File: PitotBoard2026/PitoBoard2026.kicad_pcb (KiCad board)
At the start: 2 copper layers, 8.5 x 5.5 mm, 57 parts, among them J1 RJ25, J2 ICSP, J3 Conn_01x04_Socket, J4 Conn_01x04_Pin, J5 Conn_01x04_Socket, J6 Conn_01x04_Pin, SW1 RST, U1 ATmega328PB-A, U10 MCP25625-x-SS, U2 AP7375, U4 SLIP, U7 SLIP, U8 NJW4181U3-33B, U9 BME280, Y1 16MHz, Y3 16MHz

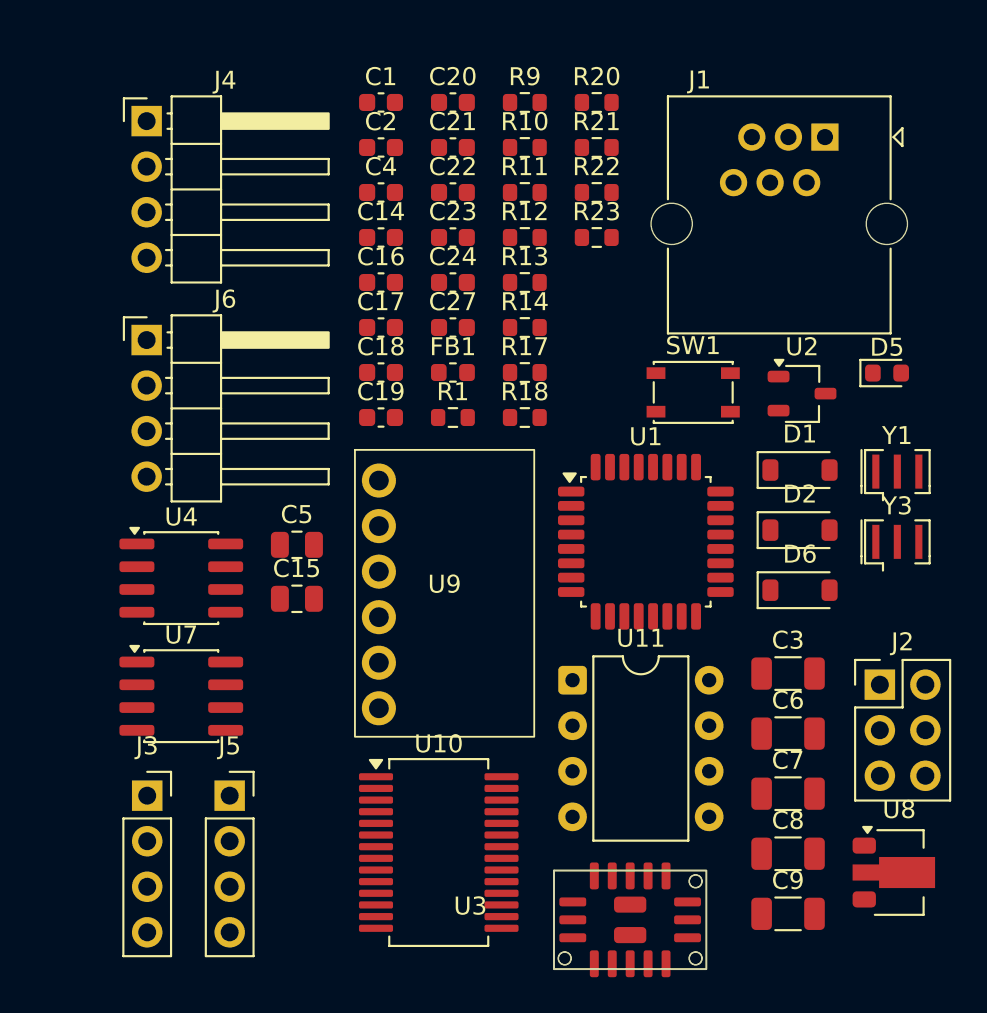
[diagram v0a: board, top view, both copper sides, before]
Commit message: Add files via upload
Edge Cuts消去
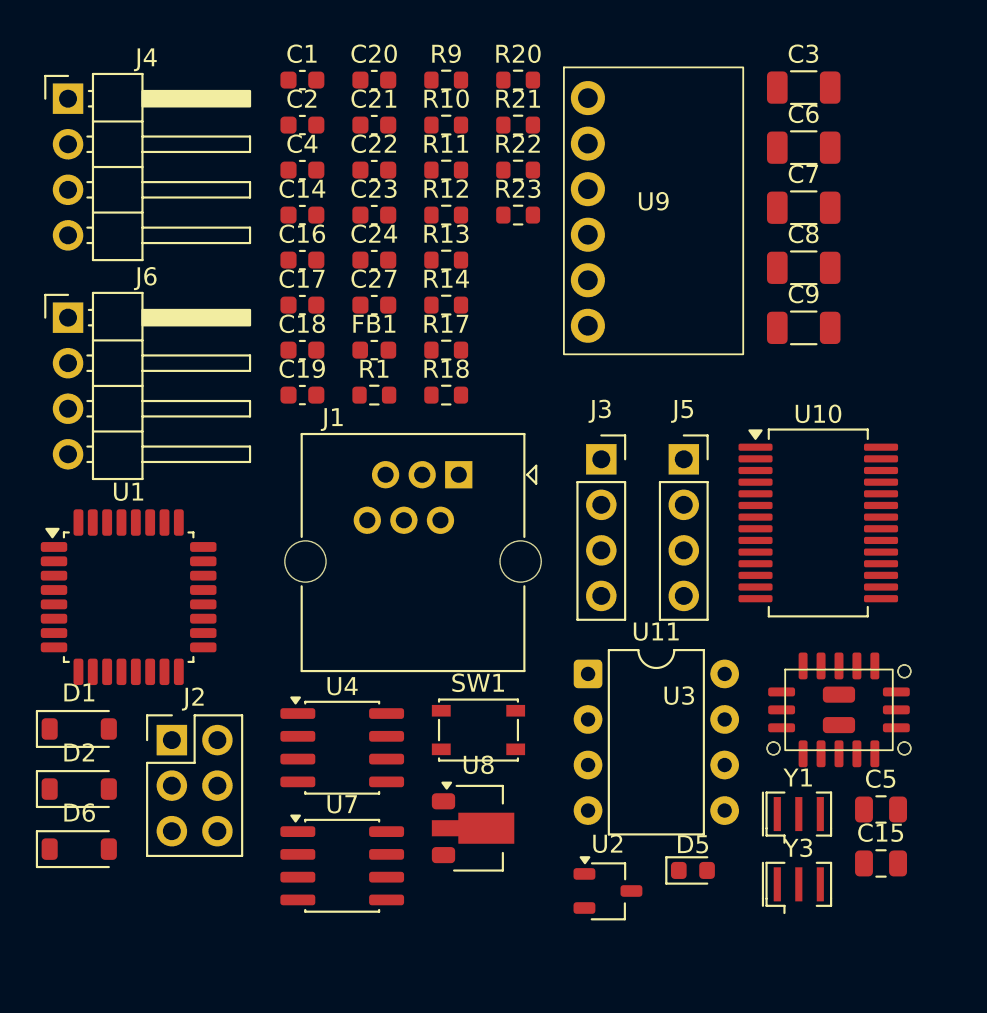
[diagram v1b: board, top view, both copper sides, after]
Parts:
- moved D1 42.7 mm to (21.3, 58.6)
- moved D6 42.7 mm to (21.3, 65.3)
- moved D2 42.7 mm to (21.3, 61.9)
- moved J2 39.6 mm to (26.5, 59.2)
- moved C15 35.8 mm to (66.0, 66.1)
- moved C5 35.8 mm to (66.0, 63.1)
- moved C7 32.7 mm to (61.7, 29.5)
- moved C9 32.7 mm to (61.7, 36.2)
- moved C3 32.7 mm to (61.7, 22.8)
- moved C6 32.7 mm to (61.7, 26.2)
- moved C8 32.7 mm to (61.7, 32.9)
- moved J3 31.5 mm to (50.4, 43.5)
- moved J5 31.5 mm to (55.0, 43.5)
- moved D5 29.8 mm to (55.5, 66.5)
- moved U2 29.8 mm to (50.8, 67.6)
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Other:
- board size 8.5 x 5.5 mm -> 8 x 5 mm

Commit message: Add files via upload
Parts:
- C15, C5: footprint Capacitor_SMD:C_0805_2012Metric -> Capacitor_SMD:C_0603_1608Metric
- C3, C6, C7, C8, C9: footprint Capacitor_SMD:C_1206_3216Metric -> Capacitor_SMD:C_0603_1608Metric
- moved C5 1.31 mm to (67.3, 63.0)
- moved C3 0.31 mm to (61.8, 22.5)
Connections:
- U11 pad 5: +5V -> (no net)

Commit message: Add files via upload
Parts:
- C1, C16, C17, C19, C20, C21, C22, C23, C24, C3, C4, C6, C7, C8, C9, D1, D2, D6, R1, R11, R13, R14, R20, R21, R22, R23, R9, U1, U10, U2, U8, Y1, Y3: moved to B.Cu
- moved D6 152.9 mm to (170.0, 101.2), turned to 90 degrees
- moved C4 152.8 mm to (170.6, 95.4)
- moved C21 144.8 mm to (163.5, 96.7)
- moved C22 142.8 mm to (163.4, 95.2)
- moved D1 141.5 mm to (154.5, 106.3), turned to 90 degrees
- moved J6 141.3 mm to (160.9, 53.4)
- moved R9 140.2 mm to (160.5, 97.0)
- moved U4 139.2 mm to (171.6, 90.9), turned to 90 degrees
- moved C2 136.6 mm to (159.5, 78.4), turned to 90 degrees
- moved C23 135.6 mm to (161.5, 85.3), turned to 90 degrees
- moved C17 133.9 mm to (161.0, 76.8), turned to 90 degrees
- moved C20 133.4 mm to (155.4, 85.3), turned to 90 degrees
- moved C16 133.3 mm to (159.5, 76.8), turned to 90 degrees
- moved C24 133.2 mm to (160.0, 85.3), turned to 90 degrees
- moved C6 131.6 mm to (167.4, 104.6), turned to 180 degrees
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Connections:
- U11 pad 5: (no net) -> +5V
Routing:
- net GND: track 0.00 -> 195.4 mm, vias 0 -> 6
- net +5V: track 0.00 -> 169.9 mm, vias 0 -> 3
- net +3V3: track 0.00 -> 88.8 mm, vias 0 -> 2
- net Net-(D1-K): track 0.00 -> 31.9 mm
- net SCL0: track 0.00 -> 31.4 mm, vias 0 -> 2
- net INT: track 0.00 -> 31.2 mm
- net SDA0: track 0.00 -> 25.6 mm, vias 0 -> 1
- net SDA3: track 0.00 -> 23.4 mm, vias 0 -> 2
- net GND1: track 0.00 -> 21.0 mm, vias 0 -> 2
- net SCL3: track 0.00 -> 20.2 mm
- net RST: track 0.00 -> 17.6 mm
- net MOSI: track 0.00 -> 17.6 mm
- net SCK: track 0.00 -> 17.5 mm, vias 0 -> 3
- net +5VA: track 0.00 -> 17.0 mm, vias 0 -> 1
- net MISO: track 0.00 -> 16.5 mm, vias 0 -> 2
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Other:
- board size 8 x 5 mm -> 34.9 x 48.5 mm

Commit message: Add files via upload
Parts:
- C1, C3, D2, R11: moved to F.Cu
- C15, FB1, R10: moved to B.Cu
- moved C14 65.9 mm to (186.3, 72.3)
- moved U7 64.2 mm to (185.7, 75.7)
- moved J4 62.6 mm to (191.1, 71.4)
- moved C15 60.6 mm to (183.1, 76.3), turned to -90 degrees
- moved J3 27.3 mm to (171.0, 72.3), turned to 0 degrees
- moved C4 25.3 mm to (145.7, 99.8)
- moved C5 25.3 mm to (147.3, 99.8)
- moved U4 25.3 mm to (146.7, 95.3)
- moved R12 20.6 mm to (144.7, 84.0), turned to -90 degrees
- moved R11 20.1 mm to (146.2, 84.0), turned to -90 degrees
- moved C17 16.7 mm to (144.3, 78.4), turned to -90 degrees
- moved SW1 16.5 mm to (148.9, 70.5), turned to 180 degrees
- moved C16 13.8 mm to (145.8, 78.4), turned to -90 degrees
- moved R14 13.3 mm to (153.1, 71.5), turned to 0 degrees
- moved R1 12.4 mm to (144.4, 72.2)
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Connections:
- C27 pad 2: Net-(J6-Pin_3) -> GND2
- J3 pad 2: SCL1 -> SCL0
- J3 pad 3: SDA1 -> SDA0
- J6 pad 3: Net-(J6-Pin_3) -> GND2
- R11 pad 1: +5VA -> +5V
- R11 pad 2: SDA2 -> SDA1
- R12 pad 1: +5VA -> +5V
- R12 pad 2: SCL2 -> SCL1
- U3 pad 1: Net-(J6-Pin_3) -> GND2
- U3 pad 10: Net-(J6-Pin_3) -> GND2
- U3 pad 11: Net-(J6-Pin_3) -> GND2
- U3 pad 17: unconnected-(U3-GND1-Pad17) -> GND2
- U3 pad 18: unconnected-(U3-GND1-Pad18) -> GND2
- U3 pad 2: Net-(J6-Pin_3) -> GND2
- U3 pad 3: Net-(J6-Pin_3) -> GND2
- U3 pad 6: Net-(J6-Pin_3) -> GND2
- U3 pad 9: Net-(J6-Pin_3) -> GND2
- U4 pad 6: SDA0 -> SDA1
- U4 pad 7: SCL0 -> SCL1
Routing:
- net +5V: track 169.9 -> 94.3 mm, vias 3 -> 7
- net +3V3: track 88.8 -> 60.8 mm, vias 2 -> 5
- net GND2: track 0.00 -> 18.9 mm, vias 0 -> 5
- net RST: track 17.6 -> 32.9 mm, vias 0 -> 2
- net SDA3: track 23.4 -> 38.3 mm, vias 2 -> 1
- net SDA1: track 7.98 -> 22.0 mm, vias 0 -> 1
- net SCL1: track 10.6 -> 24.1 mm
- net SCL3: track 20.2 -> 31.7 mm, vias 0 -> 2
- net Net-(U1-~{RESET}/PC6): track 11.8 -> 1.96 mm
- net INT: track 31.2 -> 22.4 mm, vias 0 -> 2
- net SCL0: track 31.4 -> 22.8 mm, vias 2 -> 3
- net MISO: track 16.5 -> 24.2 mm
- net Net-(J6-Pin_3): track 6.80 -> 0.00 mm
- net SDA0: track 25.6 -> 19.4 mm, vias 1 -> 4
- net Net-(J6-Pin_4): track 0.00 -> 5.67 mm
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- added copper zone on B.Cu, net GND
- added copper zone on F.Cu, net GND
- added copper zone on B.Cu, net GND1
- added copper zone on F.Cu, net GND1
- added copper zone on B.Cu, net GND2
- added copper zone on F.Cu, net GND2
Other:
- board size 34.9 x 48.5 mm -> 50.7 x 57.1 mm
